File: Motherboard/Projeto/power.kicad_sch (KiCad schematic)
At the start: 70 parts, among them J1 USB_A, J2 USB_A, J5 USB_A, J6 USB_A, P17 SCREW_TERM, P18 FAN, P38 Jumper_Receptacle, P39 Jumper_Receptacle, P40 Jumper_Receptacle, P41 Jumper_Receptacle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

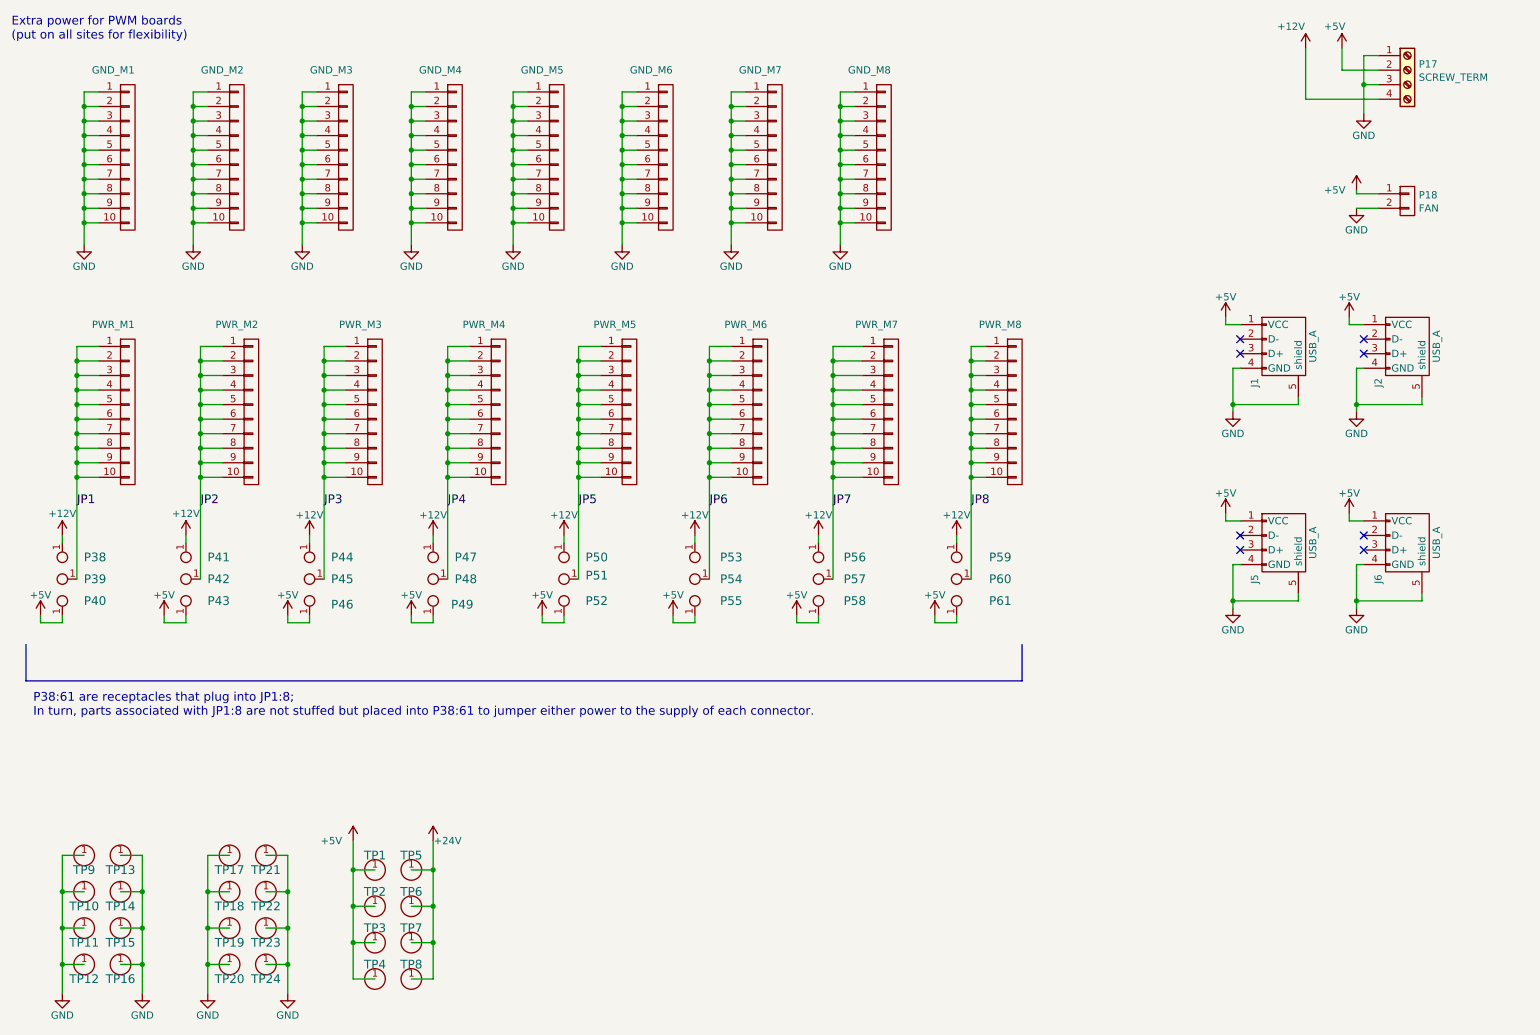
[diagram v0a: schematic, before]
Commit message: RS485 inverted terminal updated on schematic
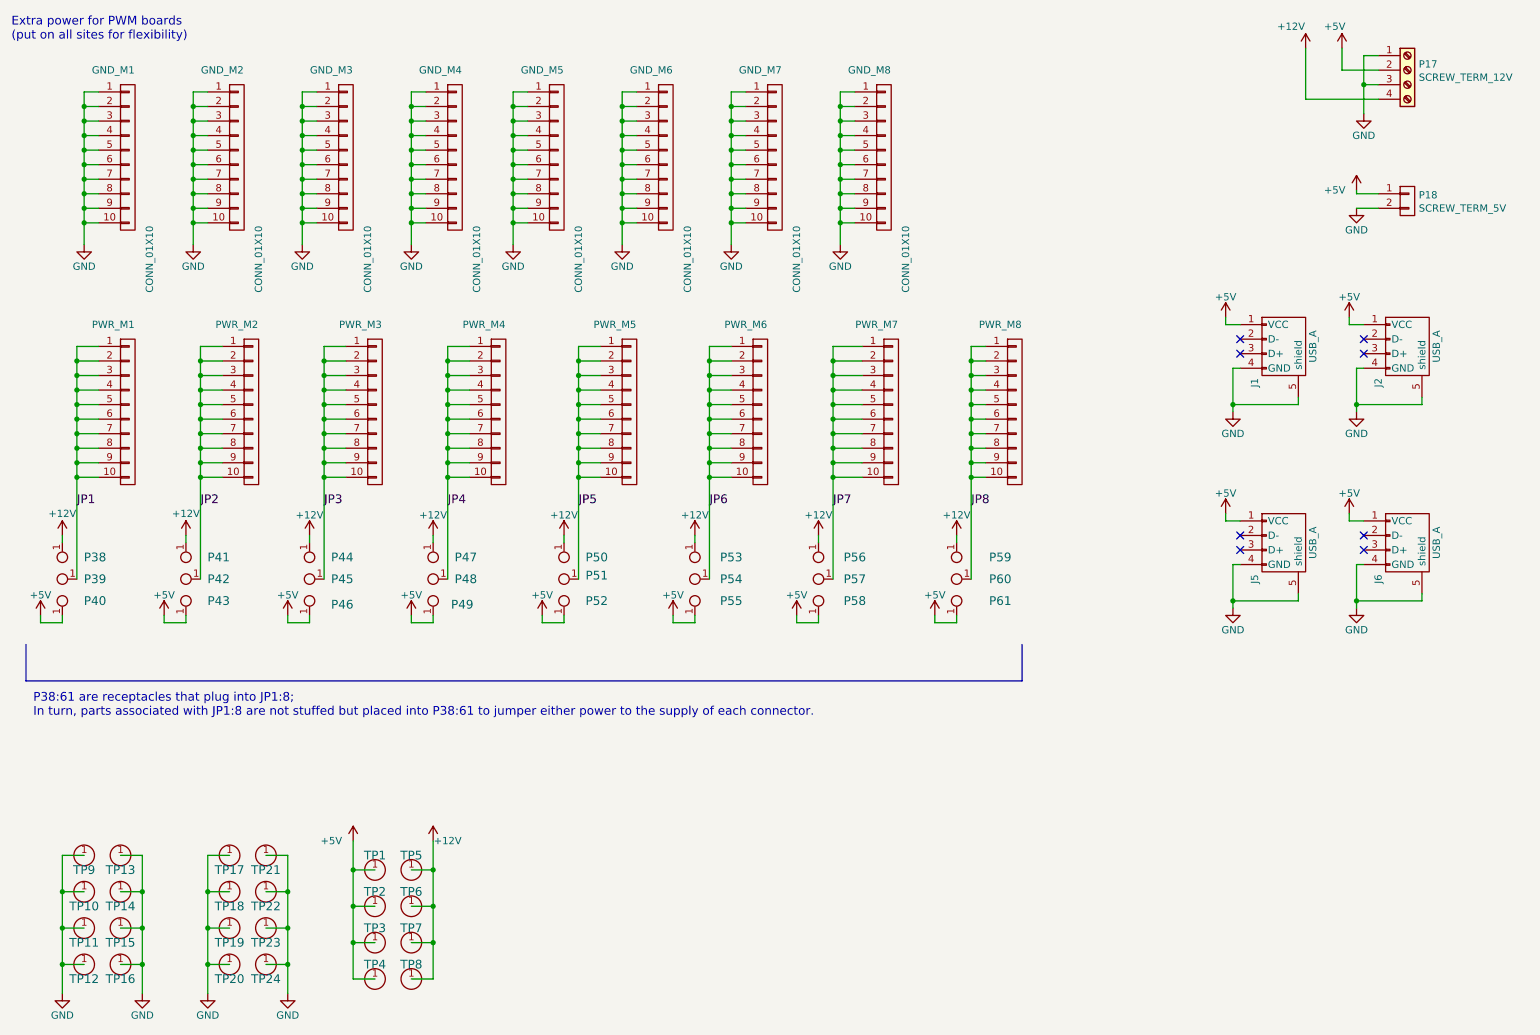
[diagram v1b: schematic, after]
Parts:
- GND_M1, GND_M2, GND_M3, GND_M4, GND_M5, GND_M6, GND_M7, GND_M8: value (none) -> CONN_01X10
- P17: value SCREW_TERM -> SCREW_TERM_12V
- P18: value FAN -> SCREW_TERM_5V
